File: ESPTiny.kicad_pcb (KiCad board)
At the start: 2 copper layers, 33 x 26.4 mm, 18 parts, among them J1 Conn_01x10_Male, J2 Conn_01x10_Male, J3 Conn_01x04_Male, U1 ESP-01v090, U2 ATtiny84-20PU, U3 MCP1700-3302E_TO92

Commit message: v1.0?
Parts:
- R2, R3: value 220 -> 1M
- moved D2 0.28 mm to (44.1, 45.3), turned to 180 degrees
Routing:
- net GND: track 3.66 -> 53.6 mm
- net Net-(D2-Pad2): track 6.69 -> 4.68 mm
- net +BATT: track 24.4 -> 25.9 mm
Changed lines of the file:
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@@
     (thickness 1.6)
     (drawings 49)
-    (tracks 133)
+    (tracks 150)
     (zones 0)
     (modules 18)
@@
   )
   (module Diode_THT:D_DO-35_SOD27_P2.54mm_Vertical_AnodeUp (layer F.Cu)
-    (at 44.323 45.212 90)
+    (at 44.069 45.339 180)
     (descr "Diode, DO-35_SOD27 series, Axial, Vertical, pin pitch=2.54mm, , length*diameter=4*2mm^2, , http://www.diodes.com/_files/packages/DO-35.pdf")
     (tags "Diode DO-35_SOD27 series Axial Vertical pin pitch 2.54mm  length 4mm diameter 2mm")
-    (fp_text reference D2 (at -0.127 -2.032 90) (layer F.SilkS)
-      (effects (font (size 1 1) (thickness 0.15)))
-    )
-    (fp_text value BAT85 (at 1.27 3.215371 90) (layer F.Fab)
+    (fp_text reference D2 (at -0.127 -2.032) (layer F.SilkS)
+      (effects (font (size 1 1) (thickness 0.15)))
+    )
+    (fp_text value BAT85 (at 1.27 3.215371) (layer F.Fab)
       (effects (font (size 1 1) (thickness 0.15)))
     )
@@
     (fp_line (start 3.59 1.25) (end 3.59 -1.25) (layer F.CrtYd) (width 0.05))
     (fp_line (start 3.59 -1.25) (end -1.25 -1.25) (layer F.CrtYd) (width 0.05))
-    (fp_text user %R (at 1.27 -2.326371 90) (layer F.Fab)
-      (effects (font (size 1 1) (thickness 0.15)))
-    )
-    (fp_text user A (at 4.34 0 90) (layer F.Fab)
-      (effects (font (size 1 1) (thickness 0.15)))
-    )
-    (fp_text user A (at 4.064 0 90) (layer F.SilkS)
-      (effects (font (size 1 1) (thickness 0.15)))
-    )
-    (pad 1 thru_hole rect (at 0 0 90) (size 1.6 1.6) (drill 0.8) (layers *.Cu *.Mask)
+    (fp_text user %R (at 1.27 -2.326371) (layer F.Fab)
+      (effects (font (size 1 1) (thickness 0.15)))
+    )
+    (fp_text user A (at 4.34 0) (layer F.Fab)
+      (effects (font (size 1 1) (thickness 0.15)))
+    )
+    (fp_text user A (at 4.064 0) (layer F.SilkS)
+      (effects (font (size 1 1) (thickness 0.15)))
+    )
+    (pad 1 thru_hole rect (at 0 0 180) (size 1.6 1.6) (drill 0.8) (layers *.Cu *.Mask)
       (net 5 +BATT))
-    (pad 2 thru_hole oval (at 2.54 0 90) (size 1.6 1.6) (drill 0.8) (layers *.Cu *.Mask)
+    (pad 2 thru_hole oval (at 2.54 0 180) (size 1.6 1.6) (drill 0.8) (layers *.Cu *.Mask)
       (net 3 "Net-(D2-Pad2)"))
     (model ${KISYS3DMOD}/Diode_THT.3dshapes/D_DO-35_SOD27_P2.54mm_Vertical_AnodeUp.wrl
@@
       (effects (font (size 0.5 0.5) (thickness 0.125)))
     )
-    (fp_text value 220 (at 1.27 2.37) (layer F.Fab)
+    (fp_text value 1M (at 1.27 2.37) (layer F.Fab)
       (effects (font (size 1 1) (thickness 0.15)))
     )
@@
       (effects (font (size 0.5 0.5) (thickness 0.125)))
     )
-    (fp_text value 220 (at 1.27 2.37) (layer F.Fab)
+    (fp_text value 1M (at 1.27 2.37) (layer F.Fab)
       (effects (font (size 1 1) (thickness 0.15)))
     )
@@
   (segment (start 70.104 45.466) (end 70.231 45.593) (width 0.5) (layer B.Cu) (net 1))
   (segment (start 70.104 42.164) (end 70.104 45.466) (width 0.5) (layer B.Cu) (net 1))
+  (segment (start 47.117 42.291) (end 47.244 42.164) (width 0.5) (layer B.Cu) (net 1))
+  (segment (start 41.021 42.291) (end 47.117 42.291) (width 0.5) (layer B.Cu) (net 1))
+  (segment (start 40.228999 47.848999) (end 43.434 51.054) (width 0.5) (layer B.Cu) (net 1))
+  (segment (start 40.228999 43.083001) (end 40.228999 47.848999) (width 0.5) (layer B.Cu) (net 1))
+  (segment (start 41.021 42.291) (end 40.228999 43.083001) (width 0.5) (layer B.Cu) (net 1))
+  (segment (start 67.437 44.831) (end 55.118 44.831) (width 0.5) (layer B.Cu) (net 1))
+  (segment (start 70.104 42.164) (end 67.437 44.831) (width 0.5) (layer B.Cu) (net 1))
+  (segment (start 46.070999 46.070999) (end 47.244 47.244) (width 0.5) (layer B.Cu) (net 1))
+  (segment (start 46.070999 43.337001) (end 46.070999 46.070999) (width 0.5) (layer B.Cu) (net 1))
+  (segment (start 47.244 42.164) (end 46.070999 43.337001) (width 0.5) (layer B.Cu) (net 1))
+  (segment (start 41.275 64.643) (end 41.021 64.897) (width 0.5) (layer B.Cu) (net 1))
+  (segment (start 41.275 60.706) (end 41.275 64.643) (width 0.5) (layer B.Cu) (net 1))
+  (segment (start 70.231 61.341) (end 67.691 61.341) (width 0.5) (layer B.Cu) (net 1))
+  (segment (start 41.021 64.897) (end 44.069 64.897) (width 0.5) (layer B.Cu) (net 1))
+  (segment (start 47.244 42.164) (end 46.355 41.275) (width 0.5) (layer B.Cu) (net 1))
   (segment (start 49.784 57.404) (end 50.546 57.404) (width 0.5) (layer F.Cu) (net 2))
   (segment (start 47.244 54.864) (end 49.784 57.404) (width 0.5) (layer F.Cu) (net 2))
@@
   (segment (start 43.528999 48.419001) (end 43.434 48.514) (width 0.25) (layer F.Cu) (net 3))
   (segment (start 43.022999 48.102999) (end 43.434 48.514) (width 0.5) (layer F.Cu) (net 3))
-  (segment (start 43.022999 43.972001) (end 43.022999 48.102999) (width 0.5) (layer F.Cu) (net 3))
-  (segment (start 44.323 42.672) (end 43.022999 43.972001) (width 0.5) (layer F.Cu) (net 3))
+  (segment (start 41.529 46.609) (end 43.434 48.514) (width 0.5) (layer F.Cu) (net 3))
+  (segment (start 41.529 45.339) (end 41.529 46.609) (width 0.5) (layer F.Cu) (net 3))
   (segment (start 57.277 60.198) (end 54.864 57.785) (width 0.25) (layer F.Cu) (net 4))
   (segment (start 59.055 60.198) (end 57.277 60.198) (width 0.25) (layer F.Cu) (net 4))
@@
   (segment (start 44.577 45.212) (end 44.784001 45.419001) (width 0.5) (layer F.Cu) (net 5))
   (segment (start 44.784001 45.673001) (end 44.323 45.212) (width 0.5) (layer F.Cu) (net 5))
-  (segment (start 44.784001 54.783999) (end 44.784001 45.673001) (width 0.5) (layer F.Cu) (net 5))
+  (segment (start 44.704 44.831) (end 44.323 45.212) (width 0.5) (layer F.Cu) (net 5))
+  (segment (start 44.784001 54.783999) (end 44.784001 46.054001) (width 0.5) (layer F.Cu) (net 5))
+  (segment (start 44.784001 46.054001) (end 44.069 45.339) (width 0.5) (layer F.Cu) (net 5))
   (segment (start 43.434 56.134) (end 44.784001 54.783999) (width 0.5) (layer F.Cu) (net 5))
-  (segment (start 44.704 44.831) (end 44.323 45.212) (width 0.5) (layer F.Cu) (net 5))
-  (segment (start 47.371 44.831) (end 44.704 44.831) (width 0.5) (layer F.Cu) (net 5))
+  (segment (start 46.863 45.339) (end 47.371 44.831) (width 0.5) (layer F.Cu) (net 5))
+  (segment (start 44.069 45.339) (end 46.863 45.339) (width 0.5) (layer F.Cu) (net 5))
   (segment (start 51.721001 64.421001) (end 52.324 65.024) (width 0.25) (layer B.Cu) (net 6))
   (segment (start 51.943998 64.643998) (end 52.324 65.024) (width 0.25) (layer F.Cu) (net 6))

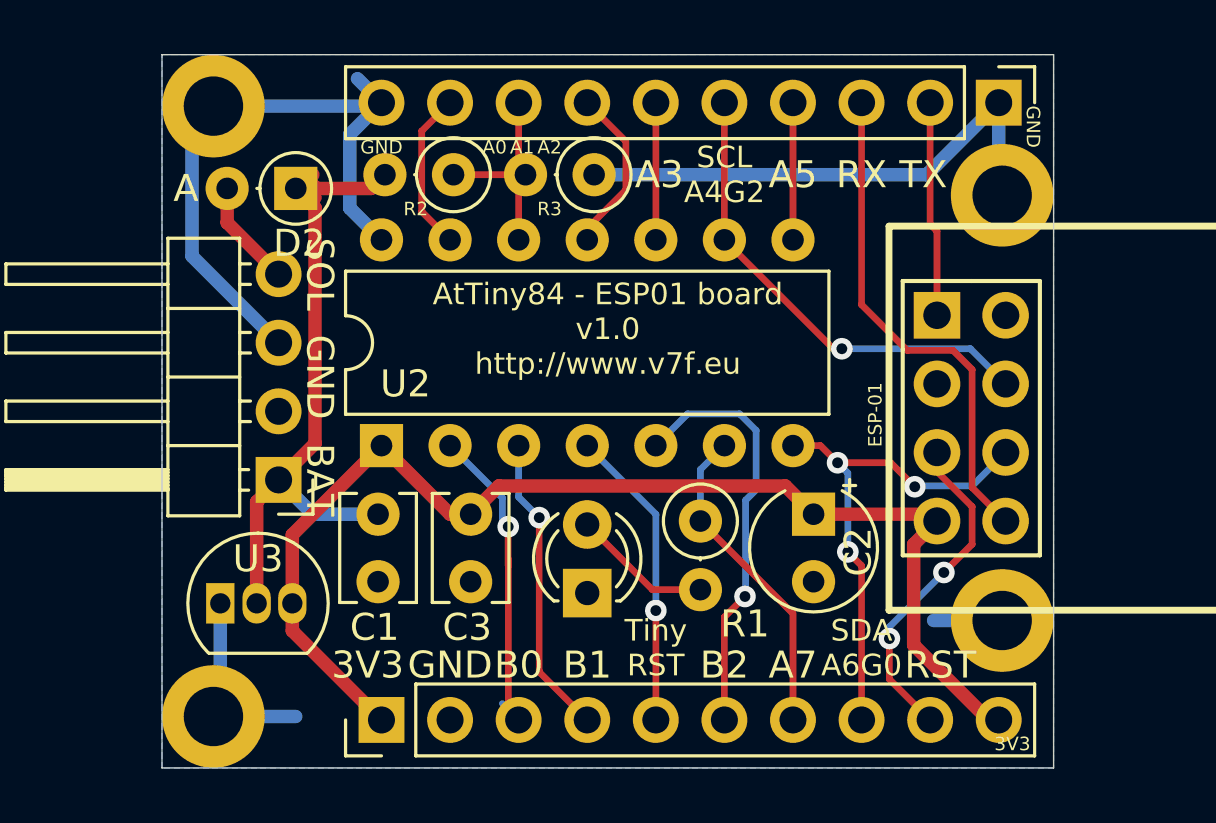
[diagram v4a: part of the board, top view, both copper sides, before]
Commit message: Add upper fills
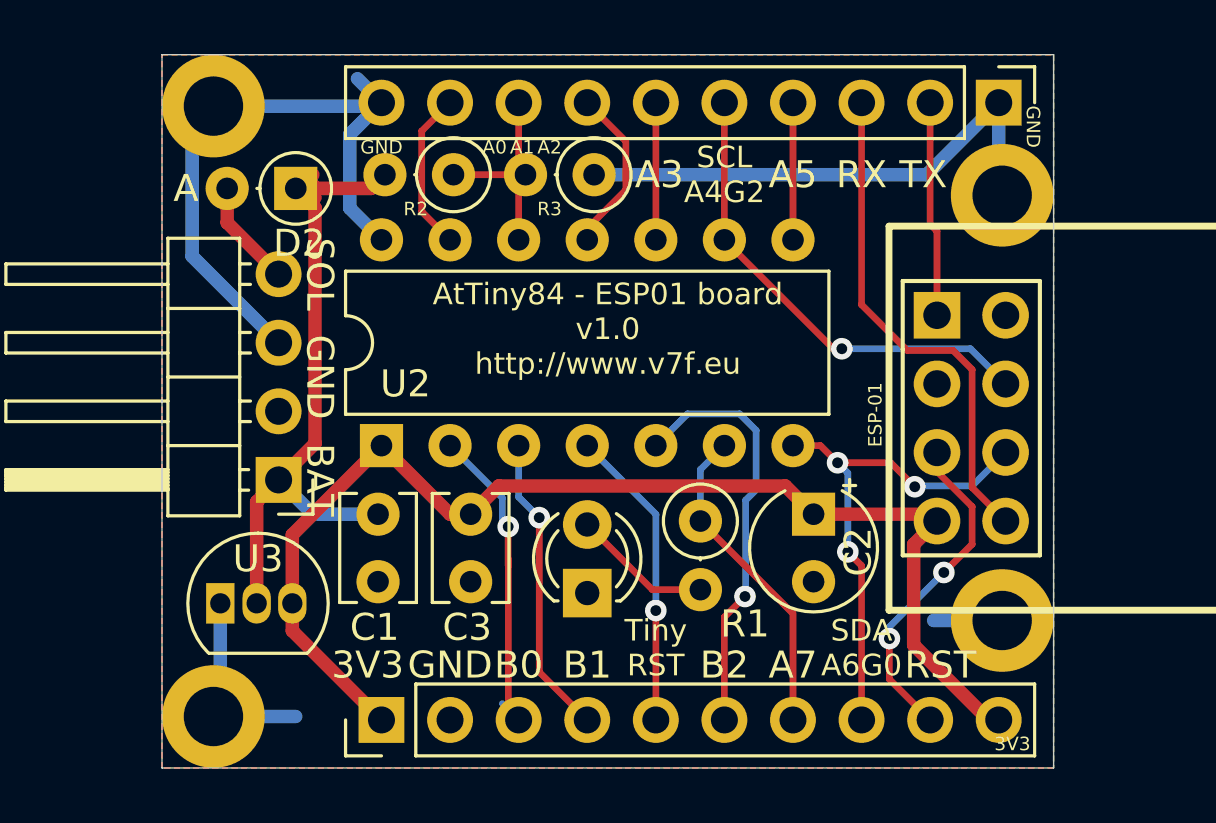
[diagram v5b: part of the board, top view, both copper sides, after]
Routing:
- added copper zone on F.Cu, net (none)
- added copper zone on F.Cu, net +3V3
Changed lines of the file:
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@@
+    )
+  )
+  (zone (net 2) (net_name +3V3) (layer F.Cu) (hatch edge 0.508)
+    (connect_pads (clearance 0.508))
+    (min_thickness 0.254)
+    (fill yes (arc_segments 32) (thermal_gap 0.508) (thermal_bridge_width 0.508))
+    (polygon
+      (pts
+        (xy 72.136 66.802) (xy 39.116 66.802) (xy 39.116 40.386) (xy 72.136 40.386)
+      )
+    )
+  )
+  (zone (net 0) (net_name "") (layer F.Cu) (hatch edge 0.508)
+    (connect_pads (clearance 0.508))
+    (min_thickness 0.254)
+    (fill yes (arc_segments 32) (thermal_gap 0.508) (thermal_bridge_width 0.508))
+    (polygon
+      (pts
+        (xy 72.136 66.802) (xy 39.116 66.802) (xy 39.116 40.386) (xy 72.136 40.386)
+      )
     )
   )
